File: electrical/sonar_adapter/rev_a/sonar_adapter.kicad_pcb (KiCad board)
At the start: 2 copper layers, 11.9 x 14.5 mm, 2 parts, among them CN1 SONAR;M1x4RA, CN2 SONAR;F1x4RA

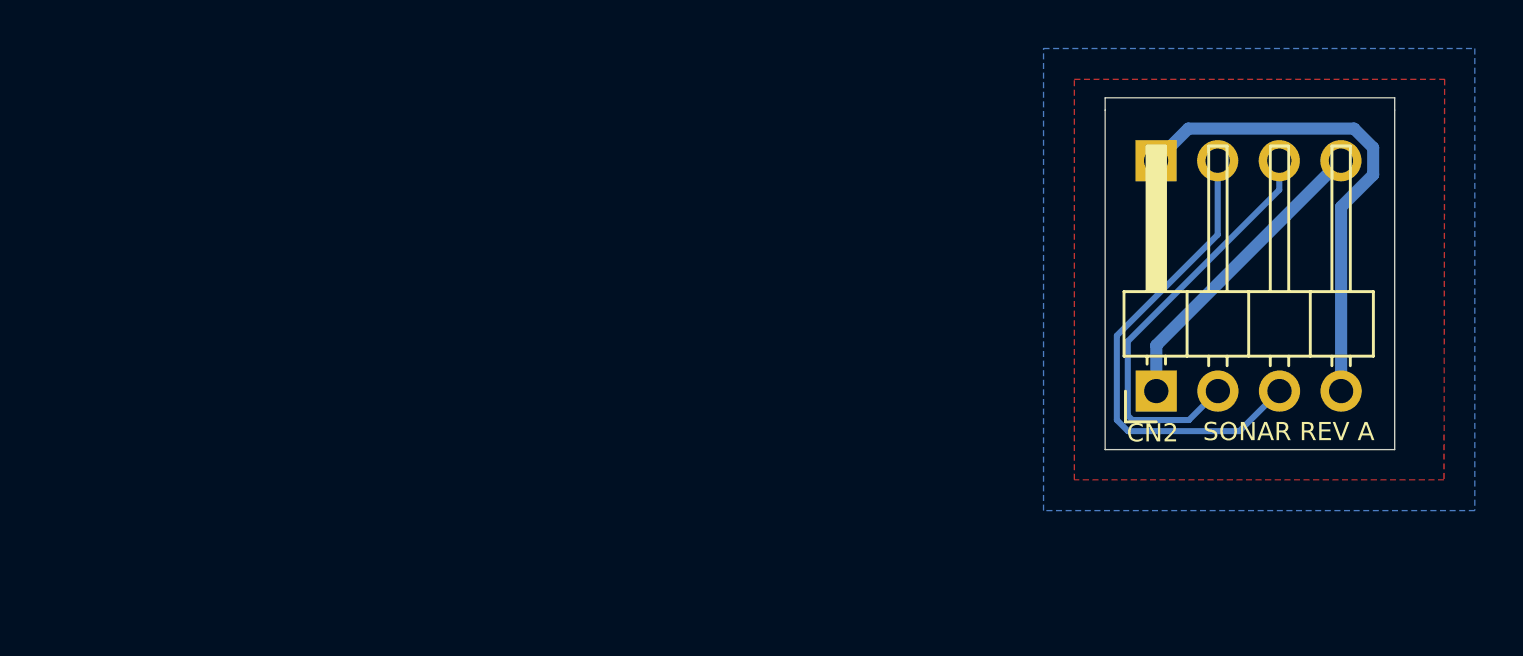
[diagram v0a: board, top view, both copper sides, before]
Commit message: Updated Sonar Adapter Rev. A.
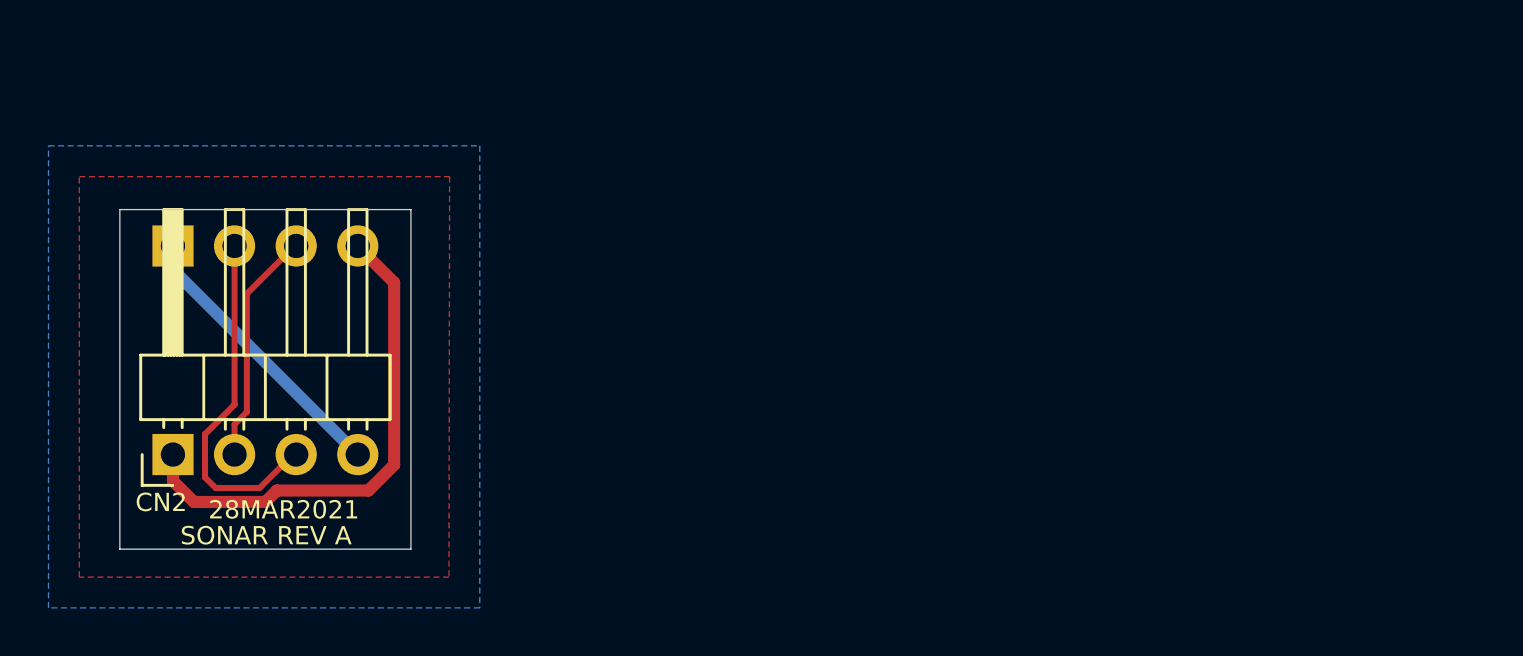
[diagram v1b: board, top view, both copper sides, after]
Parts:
- moved CN1 40.7 mm to (96.2, 94.5)
- moved CN2 40.6 mm to (96.2, 103.1)
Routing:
- net /GND: track 20.4 -> 11.8 mm
- net /VCC: track 12.6 -> 20.8 mm
- net /TRIG: track 17.4 -> 9.69 mm
- net /ECHO: track 20.0 -> 14.6 mm
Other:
- board size 11.9 x 14.5 mm -> 12 x 14 mm
- board text added: "28MAR2021"
- board text removed: "13MAR2021"
